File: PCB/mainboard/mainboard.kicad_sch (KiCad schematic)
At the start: 25 parts

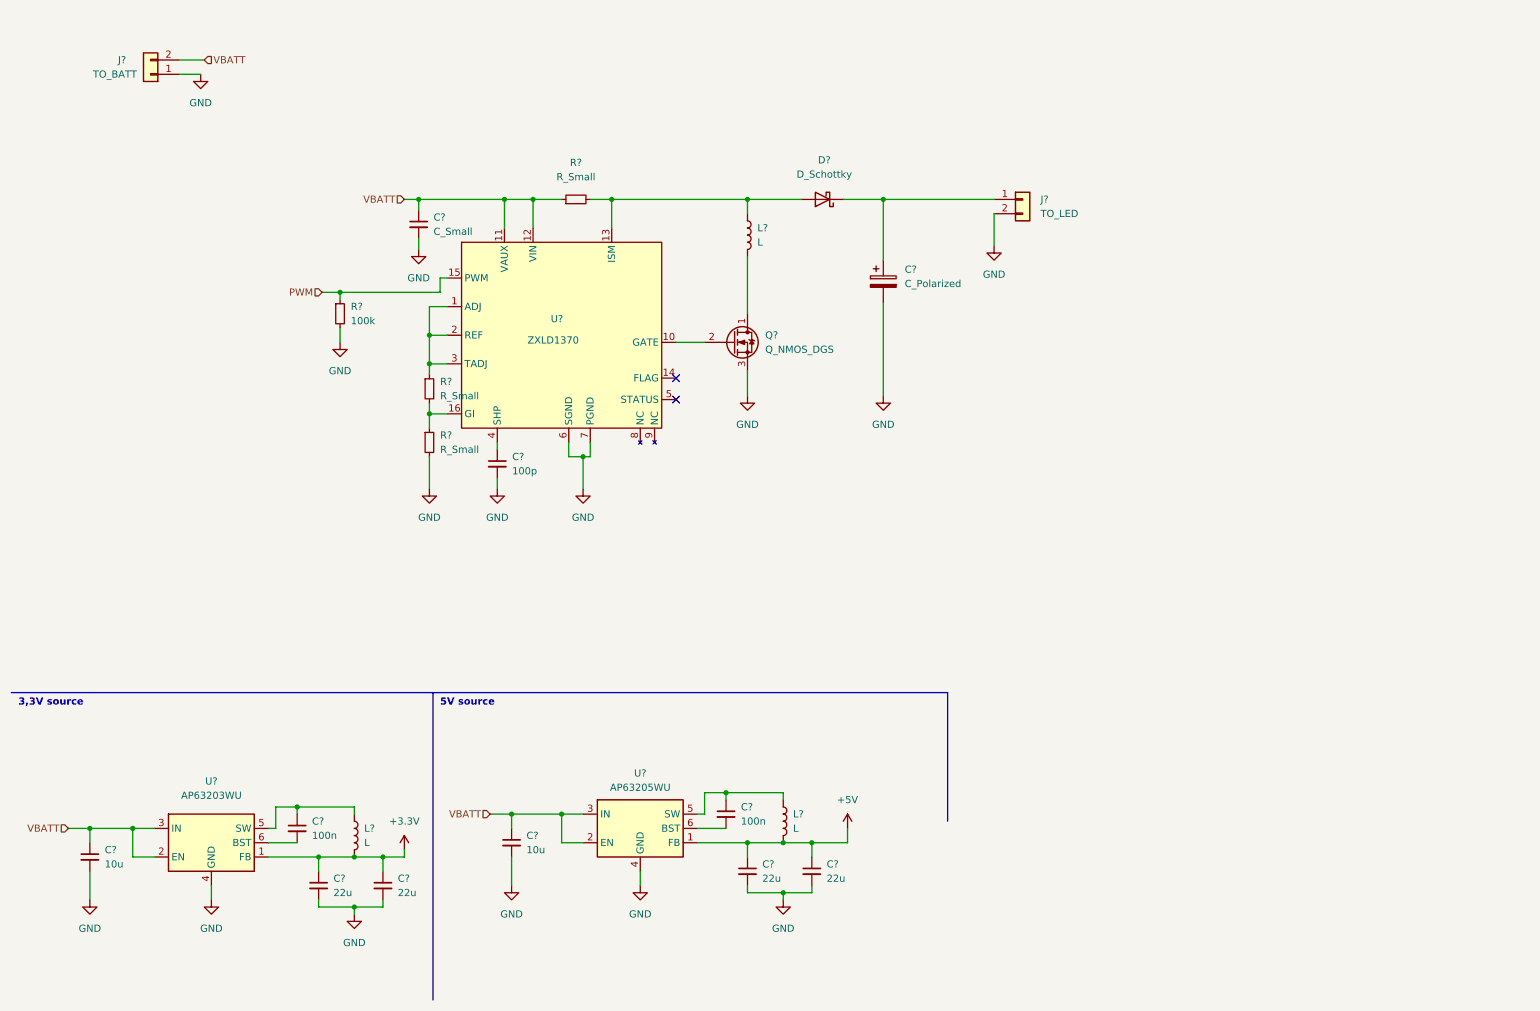
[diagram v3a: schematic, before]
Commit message: add microcontroler
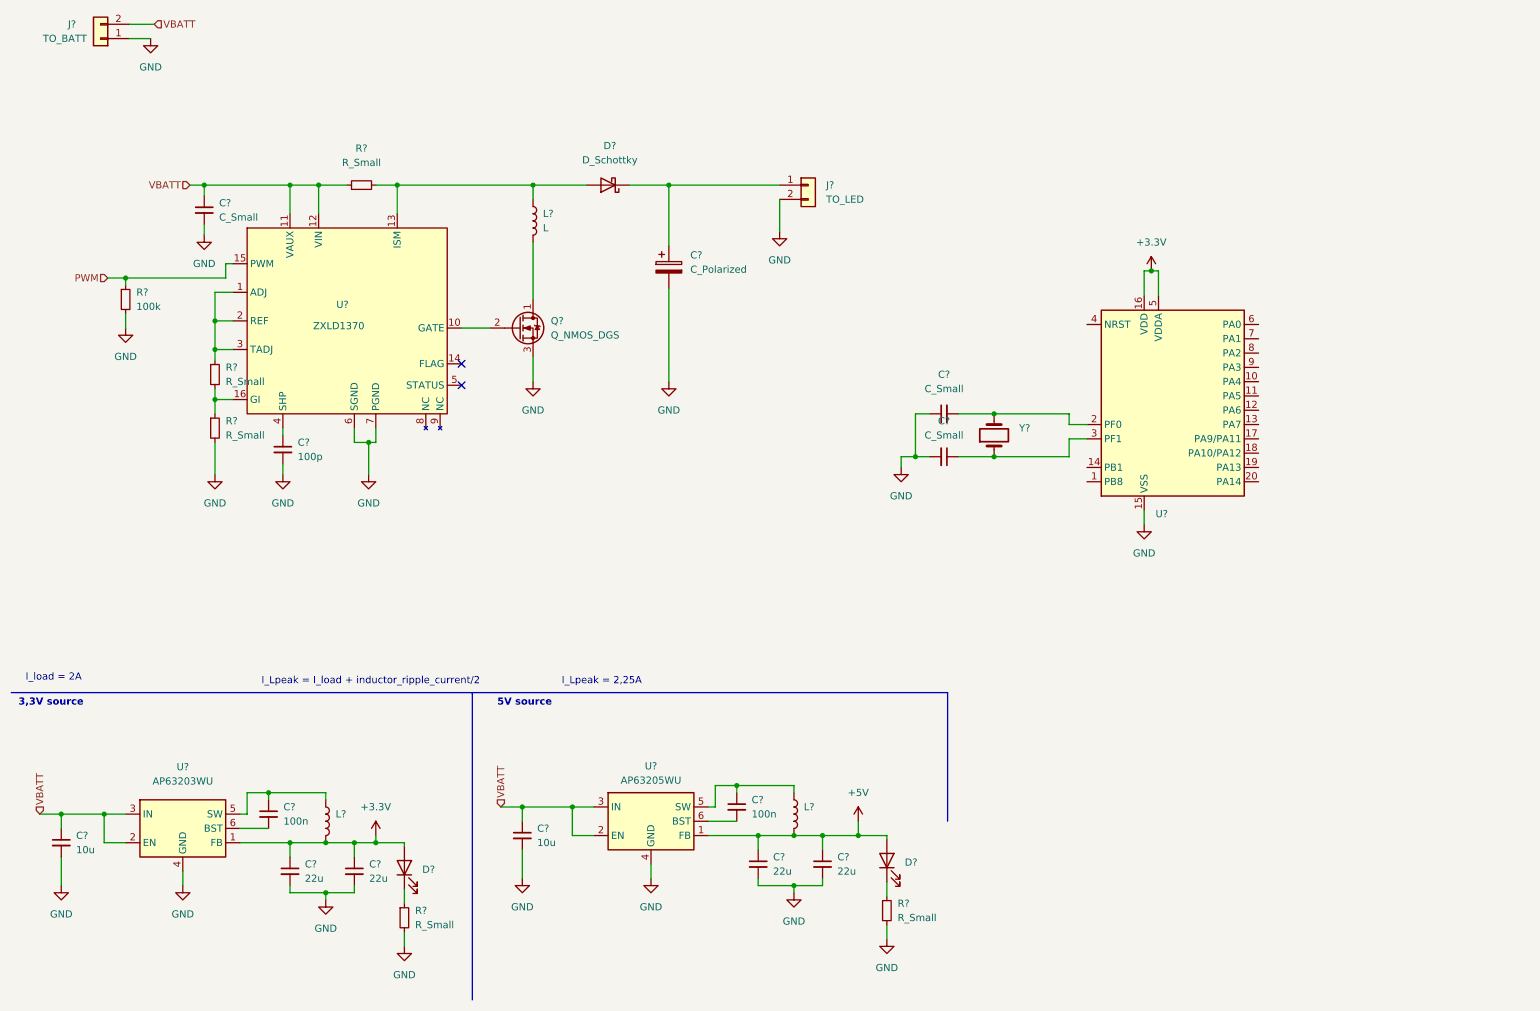
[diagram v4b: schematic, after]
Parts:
- added C? (x2): C_Small, symbol Device:C_Small
- added D? (x2): (no value), symbol Device:LED
- added R? (x2): R_Small, symbol Device:R_Small
- added U?: (no value), symbol MCU_ST_STM32F0:STM32F042F6Px
- added Y?: (no value), symbol Device:Crystal
- L? (x2): value L -> (none)
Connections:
- net +3.3V: now also D?.2 (A), U?.16 (VDD), U?.5 (VDDA)
- net +5V: now also D?.2 (A)
- net GND: now also C?.1, C?.2, R?.2, R?.2, U?.15 (VSS)
- new net: C?.2, U?.2 (PF0), Y?.2
- new net: C?.1, U?.3 (PF1), Y?.1
- new net: D?.1 (K), R?.1 (x2)
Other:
- note added: "I_Lpeak = 2,25A"
- note added: "I_Lpeak = I_load + inductor_ripple_current/2"
- note added: "I_load = 2A"
- moved on the sheet: C?, D?, J?, L?, Q?, R?, U?

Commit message: add pin configuration in STM32Cube
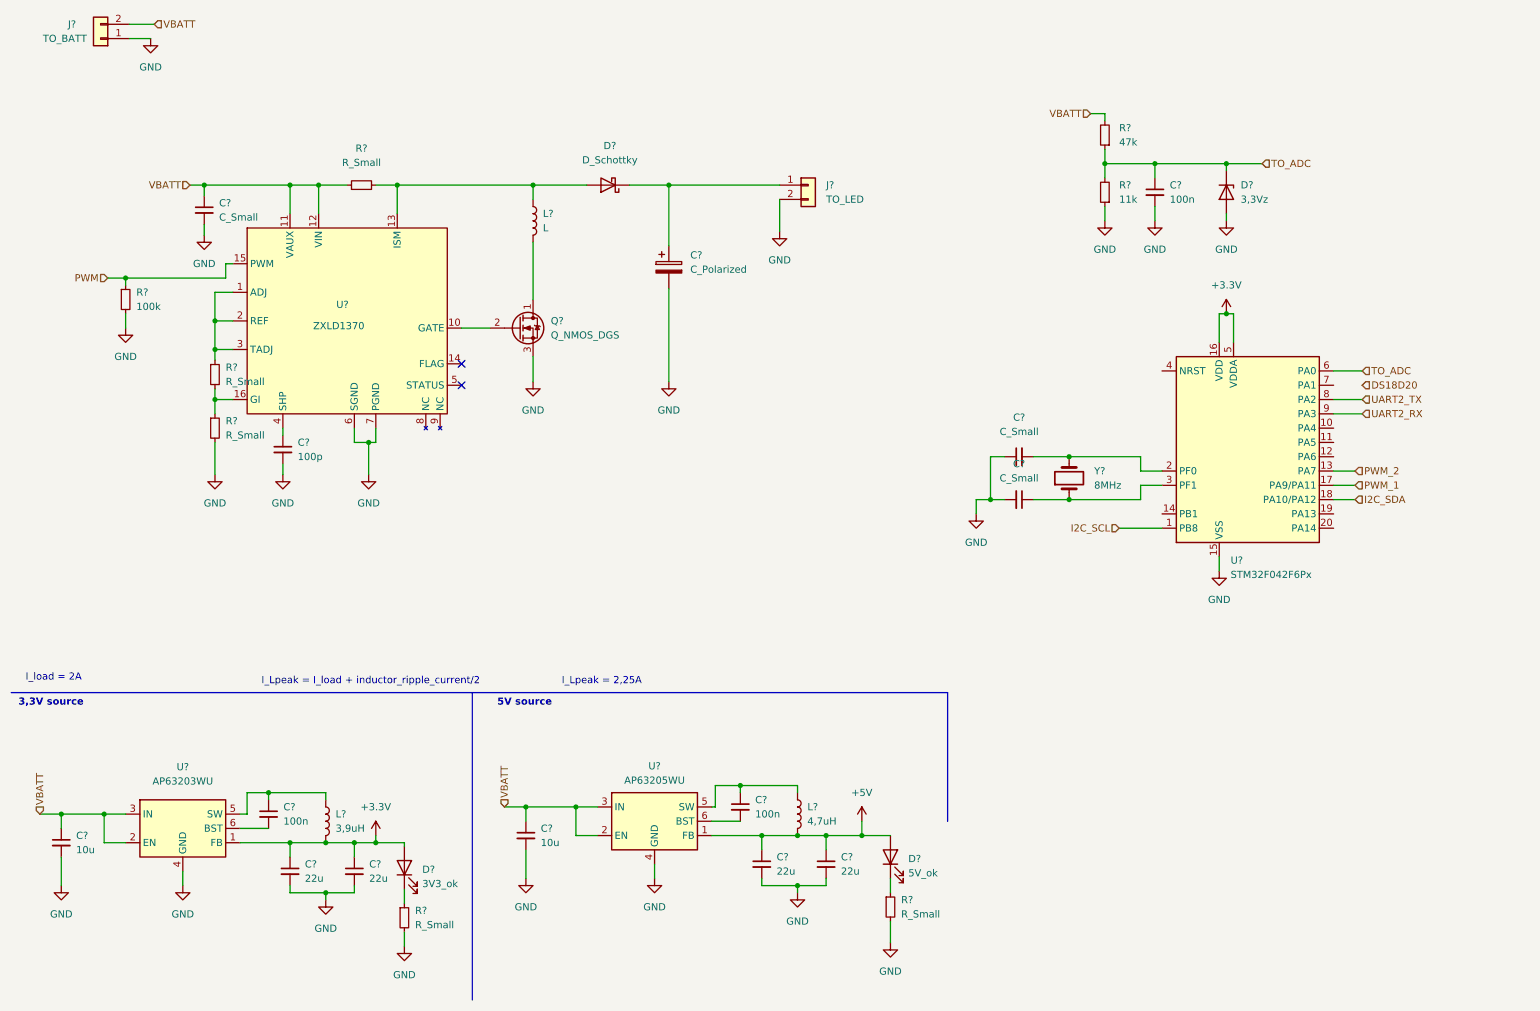
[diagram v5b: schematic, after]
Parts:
- added C?: 100n, symbol Device:C_Small
- added D?: 3,3Vz, symbol Device:D_Zener
- added R?: 47k, symbol Device:R_Small
- added R?: 11k, symbol Device:R_Small
- D?: value (none) -> 3V3_ok
- D?: value (none) -> 5V_ok
- L?: value (none) -> 4,7uH
- L?: value (none) -> 3,9uH
- U?: value (none) -> STM32F042F6Px; footprint (none) -> Package_SO:TSSOP-20_4.4x6.5mm_P0.65mm
- Y?: value (none) -> 8MHz
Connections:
- net GND: now also C?.2, D?.2 (A), R?.1
- net VBATT: now also R?.2
- net I2C_SCL: now reaches U?.1 (PB8)
- net PWM_2: now reaches U?.13 (PA7)
- net PWM_1: now reaches U?.17 (PA9/PA11)
- net I2C_SDA: now reaches U?.18 (PA10/PA12)
- net TO_ADC: now reaches U?.6 (PA0)
- net TO_ADC: now also C?.1, D?.1 (K), R?.1, R?.2
- net UART2_TX: now reaches U?.8 (PA2)
- net UART2_RX: now reaches U?.9 (PA3)
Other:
- moved on the sheet: C?, D?, L?, R?, U?, Y?

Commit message: Add connector to schamatic and change pin description in Cube
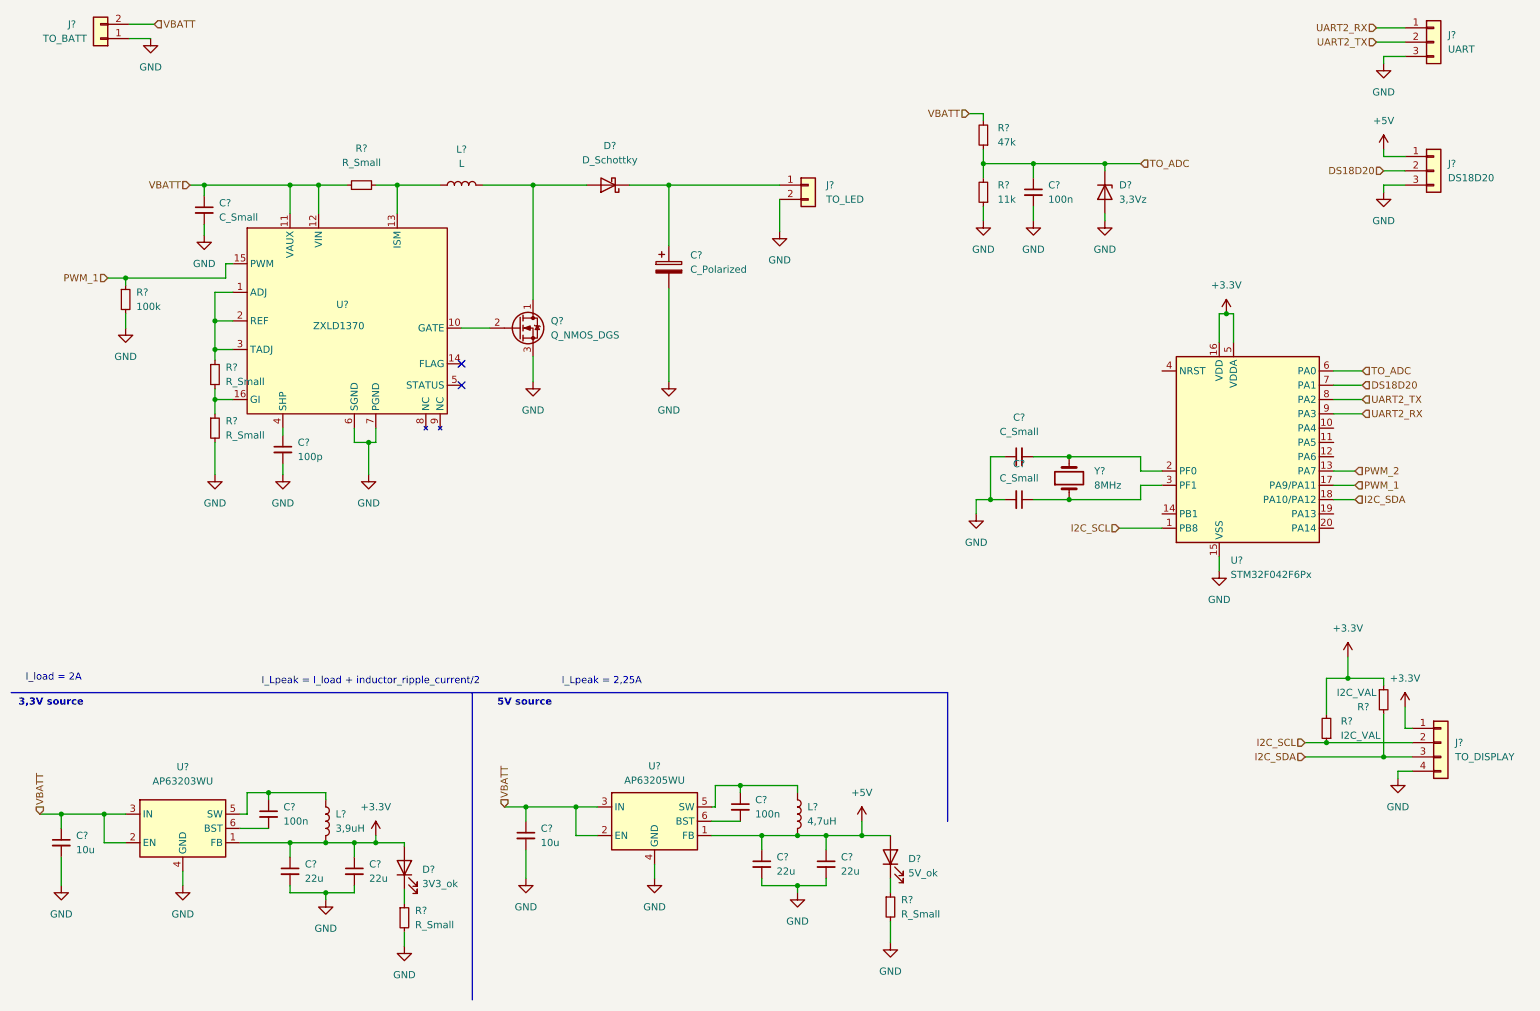
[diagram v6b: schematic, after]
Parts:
- added J?: UART, symbol Connector_Generic:Conn_01x03
- added J?: TO_DISPLAY, symbol Connector_Generic:Conn_01x04
- added J?: DS18D20, symbol Connector_Generic:Conn_01x03
- added R? (x2): I2C_VAL, symbol Device:R_Small
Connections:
- net PWM is gone; now on net PWM_1: R?.1, U?.15 (PWM)
- net +3.3V: now also J?.1 (Pin_1), R?.1, R?.2
- net +5V: now also J?.1 (Pin_1)
- net DS18D20: now also U?.7 (PA1), J?.2 (Pin_2)
- net GND: now also J?.3 (Pin_3), J?.3 (Pin_3), J?.4 (Pin_4)
- net I2C_SCL: now also J?.2 (Pin_2), R?.1
- net I2C_SDA: now also J?.3 (Pin_3), R?.2
- net UART2_RX: now also J?.1 (Pin_1)
- net UART2_TX: now also J?.2 (Pin_2)
- net at L?.1, R?.2, U?.13 (ISM): no longer D?.2 (A)
- net at L?.2, Q?.1 (D): now also D?.2 (A)
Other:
- moved on the sheet: C?, D?, L?, R?

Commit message: add calc
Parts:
- R?: value R_Small -> 0,027
- R?: value R_Small -> 82,25k
- R?: value R_Small -> 47k
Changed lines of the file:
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@@
     (in_bom yes) (on_board yes) (fields_autoplaced)
     (property "Reference" "R?" (id 0) (at 73.66 46.8122 90))
-    (property "Value" "R_Small" (id 1) (at 73.66 49.3522 90))
+    (property "Value" "0,027" (id 1) (at 73.66 49.3522 90))
     (property "Footprint" "" (id 2) (at 73.66 53.34 0)
       (effects (font (size 1.27 1.27)) hide)
@@
       (effects (font (size 1.27 1.27)) (justify left))
     )
-    (property "Value" "R_Small" (id 1) (at 49.53 88.2649 0)
+    (property "Value" "82,25k" (id 1) (at 49.53 88.2649 0)
       (effects (font (size 1.27 1.27)) (justify left))
     )
@@
   )
   (symbol (lib_id "Device:R_Small") (at 47.625 96.52 0) (unit 1)
-    (in_bom yes) (on_board yes) (fields_autoplaced)
+    (in_bom yes) (on_board yes)
     (property "Reference" "R?" (id 0) (at 49.53 95.2499 0)
       (effects (font (size 1.27 1.27)) (justify left))
     )
-    (property "Value" "R_Small" (id 1) (at 49.53 97.7899 0)
+    (property "Value" "47k" (id 1) (at 49.53 97.7899 0)
       (effects (font (size 1.27 1.27)) (justify left))
     )
@@
     )
     (path "/648f0900-74a3-41c6-b227-d63f975a0946"
-      (reference "R?") (unit 1) (value "R_Small") (footprint "")
+      (reference "R?") (unit 1) (value "0,027") (footprint "")
     )
     (path "/6c92cae8-6fcb-4b28-9679-24dcda080db9"
@@
     )
     (path "/b51b23e0-9454-40c4-b732-6059bb2fc6e1"
-      (reference "R?") (unit 1) (value "R_Small") (footprint "")
+      (reference "R?") (unit 1) (value "82,25k") (footprint "")
     )
     (path "/cc9c1450-7b97-4079-acc5-f11bfc15cddb"
@@
     )
     (path "/d11007e4-82dc-4aa4-88c2-79d141c915d4"
-      (reference "R?") (unit 1) (value "R_Small") (footprint "")
+      (reference "R?") (unit 1) (value "47k") (footprint "")
     )
     (path "/e384bd8b-34f2-464f-b802-f02f9a2f18c4"
